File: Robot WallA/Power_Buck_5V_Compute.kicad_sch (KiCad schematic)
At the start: 13 parts

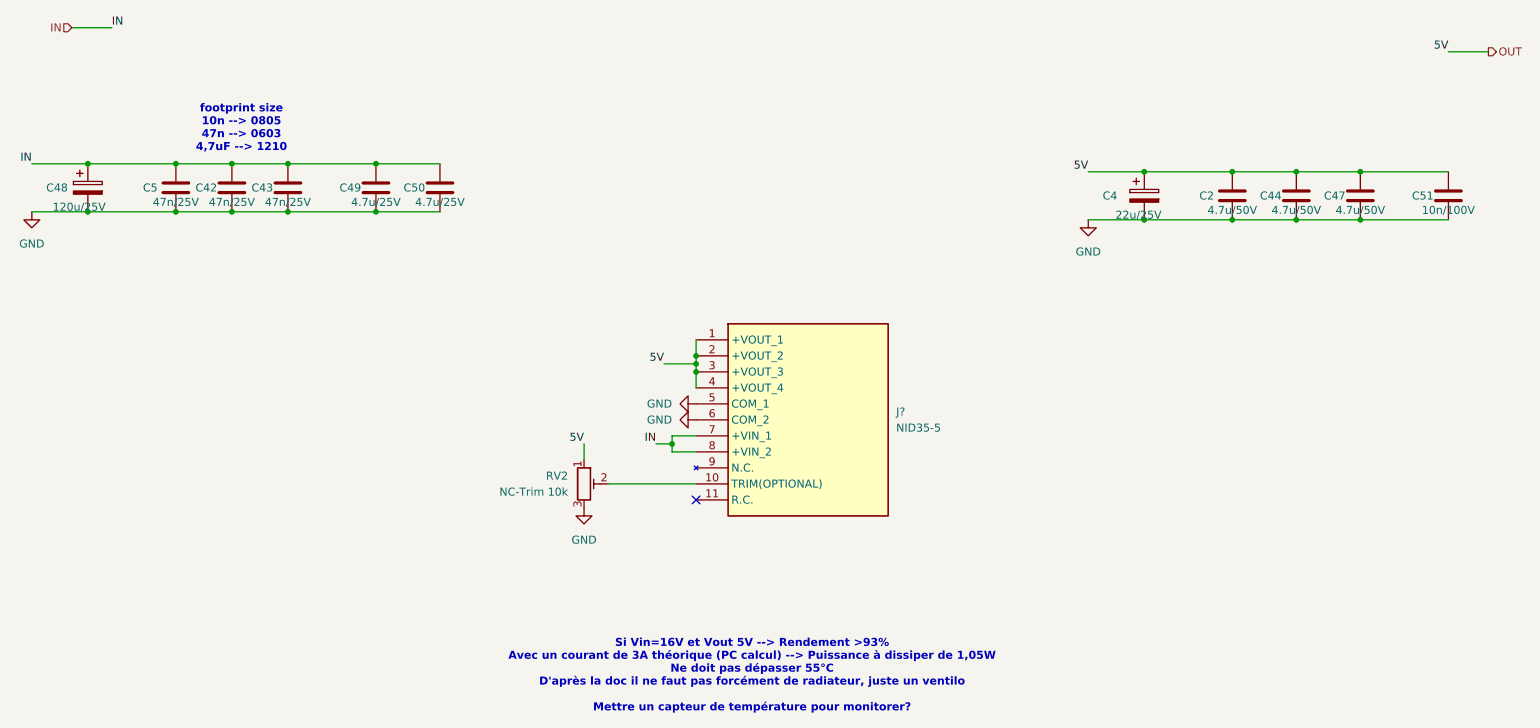
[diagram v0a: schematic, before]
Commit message: Continued to link MCU pins, Added a sheet for servomotors and optional 2 DC motors.
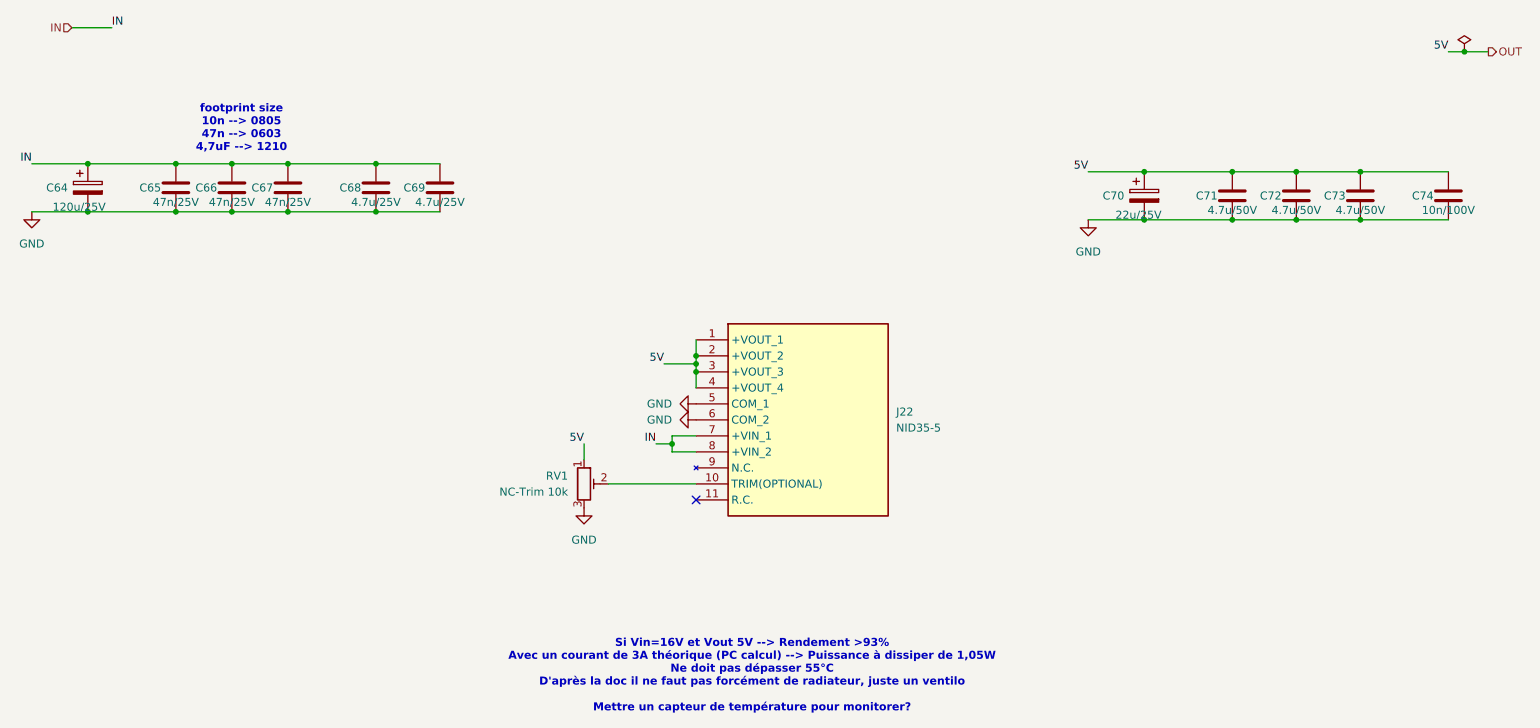
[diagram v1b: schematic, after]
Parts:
- removed C2, C44, C47: 4.7u/50V, symbol Device:C
- removed C4: 22u/25V, symbol Device:C_Polarized
- removed C42, C43, C5: 47n/25V, symbol Device:C
- removed C48: 120u/25V, symbol Device:C_Polarized
- removed C49, C50: 4.7u/25V, symbol Device:C
- removed C51: 10n/100V, symbol Device:C
- removed J?: NID35-5, NID355, symbol SamacSys_Parts:NID35-5
- removed RV2: NC-Trim 10k, symbol Device:R_Potentiometer_Trim
- added C64: 120u/25V, symbol Device:C_Polarized
- added C65, C66, C67: 47n/25V, symbol Device:C
- added C68, C69: 4.7u/25V, symbol Device:C
- added C70: 22u/25V, symbol Device:C_Polarized
- added C71, C72, C73: 4.7u/50V, symbol Device:C
- added C74: 10n/100V, symbol Device:C
- added J22: NID35-5, NID355, symbol SamacSys_Parts:NID35-5
- added RV1: NC-Trim 10k, symbol Device:R_Potentiometer_Trim
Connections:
- net GND: now also C64.2, C65.2, C66.2, C67.2, C68.2, C69.2, C70.2, C71.2, C72.2, C73.2, C74.2, J22.5 (COM_1), J22.6 (COM_2), RV1.3
- net IN: now also C64.1, C65.1, C66.1, C67.1, C68.1, C69.1, J22.7 (+VIN_1), J22.8 (+VIN_2)
- net OUT: now also C70.1, C71.1, C72.1, C73.1, C74.1, J22.1 (+VOUT_1), J22.2 (+VOUT_2), J22.3 (+VOUT_3), J22.4 (+VOUT_4), RV1.1
- new net: J22.10 (TRIM(OPTIONAL)), RV1.2

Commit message: Defined every footprints
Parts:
- C40: renamed from C64; value 120u/25V -> 120uF/25V; footprint (none) -> SamacSys_Parts:EEE0JA331XP; Manufacturer_Part_Number (none) -> EEE-FNV121XUP
- C41: renamed from C65; value 47n/25V -> 47nF/25V; footprint (none) -> Capacitor_SMD:C_0603_1608Metric_Pad1.08x0.95mm_HandSolder
- C42: renamed from C66; value 47n/25V -> 47nF/25V; footprint (none) -> Capacitor_SMD:C_0603_1608Metric_Pad1.08x0.95mm_HandSolder
- C43: renamed from C67; value 47n/25V -> 47nF/25V; footprint (none) -> Capacitor_SMD:C_0603_1608Metric_Pad1.08x0.95mm_HandSolder
- C44: renamed from C68; value 4.7u/25V -> 4.7uF/25V; footprint (none) -> Capacitor_SMD:C_1210_3225Metric_Pad1.33x2.70mm_HandSolder
- C45: renamed from C69; value 4.7u/25V -> 4.7uF/25V; footprint (none) -> Capacitor_SMD:C_1210_3225Metric_Pad1.33x2.70mm_HandSolder
- C46: renamed from C70; value 22u/25V -> 22uF/25V; footprint (none) -> Capacitor_SMD:C_0805_2012Metric_Pad1.18x1.45mm_HandSolder
- C47: renamed from C71; value 4.7u/50V -> 4.7uF/50V; footprint (none) -> Capacitor_SMD:C_0805_2012Metric_Pad1.18x1.45mm_HandSolder
- C48: renamed from C72; value 4.7u/50V -> 4.7uF/50V; footprint (none) -> Capacitor_SMD:C_0805_2012Metric_Pad1.18x1.45mm_HandSolder
- C49: renamed from C73; value 4.7u/50V -> 4.7uF/50V; footprint (none) -> Capacitor_SMD:C_0805_2012Metric_Pad1.18x1.45mm_HandSolder
- C50: renamed from C74; value 10n/100V -> 10nF/50V; footprint (none) -> Capacitor_SMD:C_0805_2012Metric_Pad1.18x1.45mm_HandSolder
- J11: renamed from J22; footprint NID355 -> SamacSys_Parts:NID355; Arrow Part Number NID35-5 -> (none); Arrow Price/Stock https://www.arrow.com/en/products/nid35-5/mean-well-enterpr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 -> (none); Height 13 -> (none); Manufacturer_Name Mean Well -> (none); Mouser Part Number 709-NID35-5 -> (none); Mouser Price/Stock https://www.mouser.co.uk/ProductDetail/MEAN-WELL/NID35-5?qs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 -> (none)
- RV1: value NC-Trim 10k -> Trim 10k; footprint (none) -> SamacSys_Parts:TC33X2503E; now not fitted

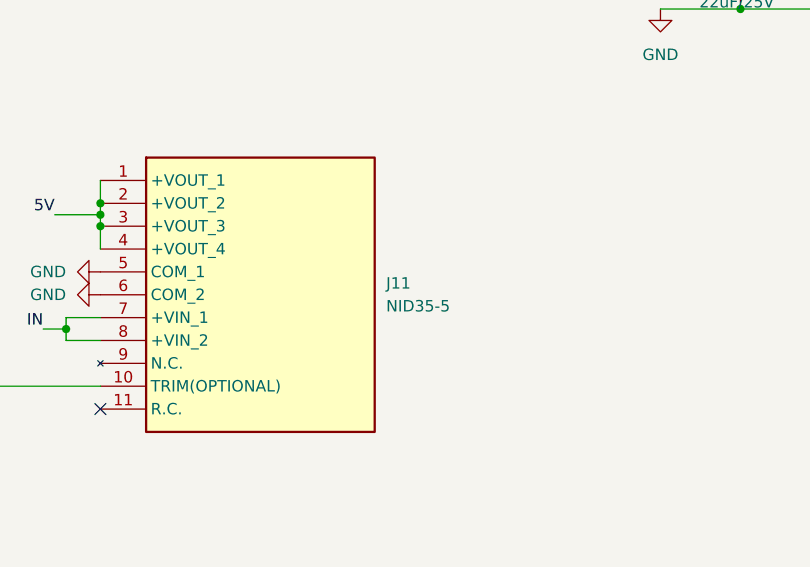
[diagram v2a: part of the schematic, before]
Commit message: Updated USB UART converter, Linked telemeter sensors.
Updated components indicators
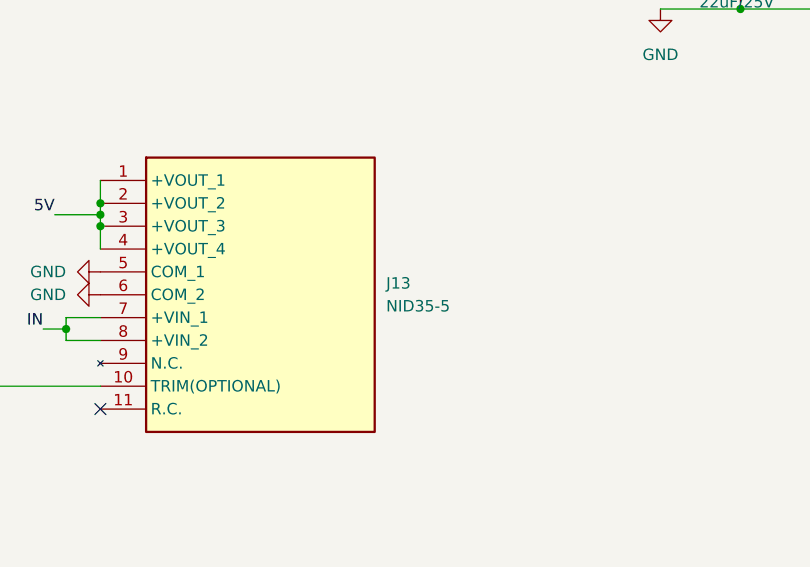
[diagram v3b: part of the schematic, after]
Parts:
- RV1: Manufacturer_Part_Number (none) -> TC33X2503E
- renumbered J11 to J13
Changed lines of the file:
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@@
+			)
+		)
+		(property "Manufacturer_Part_Number" "TC33X2503E"
+			(at 120.65 97.79 0)
+			(effects
+				(font
+					(size 1.27 1.27)
+				)
+				(hide yes)
 			)
 		)
@@
 		(dnp no)
 		(fields_autoplaced yes)
-		(property "Reference" "#PWR057"
+		(property "Reference" "#PWR059"
 			(at 132.08 87.63 0)
 			(effects
@@
 			(project "PCB"
 				(path "/117fd49e-499d-4b54-b58c-f6b538ecca4a/d5f4dab0-e2de-4083-971d-4b1eb9c8d4bb/690dff04-39a8-47af-a544-90bdf7825c98"
-					(reference "#PWR057")
+					(reference "#PWR059")
 					(unit 1)
 				)
@@
 		(dnp no)
 		(fields_autoplaced yes)
-		(property "Reference" "#PWR058"
+		(property "Reference" "#PWR060"
 			(at 120.65 107.95 0)
 			(effects
@@
 			(project "PCB"
 				(path "/117fd49e-499d-4b54-b58c-f6b538ecca4a/d5f4dab0-e2de-4083-971d-4b1eb9c8d4bb/690dff04-39a8-47af-a544-90bdf7825c98"
-					(reference "#PWR058")
+					(reference "#PWR060")
 					(unit 1)
 				)
@@
 		(dnp no)
 		(fields_autoplaced yes)
-		(property "Reference" "#PWR054"
+		(property "Reference" "#PWR056"
 			(at 33.02 60.96 0)
 			(effects
@@
 			(project "PCB"
 				(path "/117fd49e-499d-4b54-b58c-f6b538ecca4a/d5f4dab0-e2de-4083-971d-4b1eb9c8d4bb/690dff04-39a8-47af-a544-90bdf7825c98"
-					(reference "#PWR054")
+					(reference "#PWR056")
 					(unit 1)
 				)
@@
 		(dnp no)
 		(fields_autoplaced yes)
-		(property "Reference" "J11"
+		(property "Reference" "J13"
 			(at 170.18 86.3599 0)
 			(effects
@@
 			(project "PCB"
 				(path "/117fd49e-499d-4b54-b58c-f6b538ecca4a/d5f4dab0-e2de-4083-971d-4b1eb9c8d4bb/690dff04-39a8-47af-a544-90bdf7825c98"
-					(reference "J11")
+					(reference "J13")
 					(unit 1)
 				)
@@
 		(dnp no)
 		(fields_autoplaced yes)
-		(property "Reference" "#PWR056"
+		(property "Reference" "#PWR058"
 			(at 132.08 85.09 0)
 			(effects
@@
 			(project "PCB"
 				(path "/117fd49e-499d-4b54-b58c-f6b538ecca4a/d5f4dab0-e2de-4083-971d-4b1eb9c8d4bb/690dff04-39a8-47af-a544-90bdf7825c98"
-					(reference "#PWR056")
+					(reference "#PWR058")
 					(unit 1)
 				)
@@
 		(dnp no)
 		(fields_autoplaced yes)
-		(property "Reference" "#PWR055"
+		(property "Reference" "#PWR057"
 			(at 200.66 62.23 0)
 			(effects
@@
 			(project "PCB"
 				(path "/117fd49e-499d-4b54-b58c-f6b538ecca4a/d5f4dab0-e2de-4083-971d-4b1eb9c8d4bb/690dff04-39a8-47af-a544-90bdf7825c98"
-					(reference "#PWR055")
-					(unit 1)
-				)
+					(reference "#PWR057")
+					(unit 1)
+				)

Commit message: Continue to route
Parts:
- C46: footprint Capacitor_SMD:C_0805_2012Metric_Pad1.18x1.45mm_HandSolder -> SamacSys_Parts:EEE1AA220WR; Height (none) -> 5.5; Manufacturer_Part_Number (none) -> EEE-FN1E220R

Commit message: Reworked 12V and 5V power supplies, continue routing
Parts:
- removed C40: 120uF/25V, SamacSys_Parts:EEE0JA331XP, symbol Device:C_Polarized
- removed C41, C42, C43: 47nF/25V, Capacitor_SMD:C_0603_1608Metric_Pad1.08x0.95mm_HandSolder, symbol Device:C
- removed C44, C45: 4.7uF/25V, Capacitor_SMD:C_1210_3225Metric_Pad1.33x2.70mm_HandSolder, symbol Device:C
- removed C46: 22uF/25V, SamacSys_Parts:EEE1AA220WR, symbol Device:C_Polarized
- removed C47, C48, C49: 4.7uF/50V, Capacitor_SMD:C_0805_2012Metric_Pad1.18x1.45mm_HandSolder, symbol Device:C
- removed C50: 10nF/50V, Capacitor_SMD:C_0805_2012Metric_Pad1.18x1.45mm_HandSolder, symbol Device:C
- removed J13: NID35-5, SamacSys_Parts:NID355, symbol SamacSys_Parts:NID35-5
- removed RV1: Trim 10k, SamacSys_Parts:TC33X2503E, symbol Device:R_Potentiometer_Trim
- added C51: 330uF, SamacSys_Parts:CAPPRD500W65D1000H1800, symbol Device:C_Polarized
- added C52, C53: 4.7uF/50V, Capacitor_SMD:C_1210_3225Metric_Pad1.33x2.70mm_HandSolder, symbol Device:C
- added C54: 10nF/50V, Capacitor_SMD:C_0805_2012Metric_Pad1.18x1.45mm_HandSolder, symbol Device:C
- added C55: 2.2uF/50V, Capacitor_SMD:C_1210_3225Metric_Pad1.33x2.70mm_HandSolder, symbol Device:C
- added C56, C57, C58: 47nF/25V, Capacitor_SMD:C_0603_1608Metric_Pad1.08x0.95mm_HandSolder, symbol Device:C
- added C59, C60: 4.7uF/25V, Capacitor_SMD:C_1210_3225Metric_Pad1.33x2.70mm_HandSolder, symbol Device:C
- added D16: LED_RED, LED_SMD:LED_0603_1608Metric, symbol Device:LED
- added JP14: Closed, Jumper:SolderJumper-2_P1.3mm_Bridged_RoundedPad1.0x1.5mm, symbol Jumper:Jumper_2_Bridged
- added JP15: Open, Jumper:SolderJumper-2_P1.3mm_Open_RoundedPad1.0x1.5mm, symbol Jumper:Jumper_2_Open
- added Q1: BSS138, Package_TO_SOT_SMD:SOT-23, symbol Transistor_FET:BSS138
- added R31: 1.6k, Resistor_SMD:R_0603_1608Metric_Pad0.98x0.95mm_HandSolder, symbol Device:R
- added R32: 21k, Resistor_SMD:R_0603_1608Metric_Pad0.98x0.95mm_HandSolder, symbol Device:R
- added R40: 10k, Resistor_SMD:R_0603_1608Metric_Pad0.98x0.95mm_HandSolder, symbol Device:R
- added RV2: Trim 2k, SamacSys_Parts:TC42X2202E, symbol Device:R_Potentiometer_Trim
- added U10: PTN78060W_EUW-7, Module:Texas_EUW_R-PDSS-T7_THT, symbol Converter_DCDC:PTN78060W_EUW-7
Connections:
- net GND: now also C51.2, C52.2, C53.2, C54.2, C55.2, C56.2, C57.2, C58.2, C59.2, C60.2, JP14.1 (A), Q1.2 (S), R31.2, R40.2, RV2.2, U10.1 (GND), U10.7 (GND)
- net IN: now also C55.1, C56.1, C57.1, C58.1, C59.1, C60.1, U10.2 (VI)
- net OUT: now also C51.1, C52.1, C53.1, C54.1, D16.2 (A), U10.5 (VO_Sense), U10.6 (VO)
- new net: JP15.2 (B), RV2.1
- new net: D16.1 (K), R31.1
- new net: JP14.2 (B), JP15.1 (A), R32.2
- new net: Q1.3 (D), U10.3 (~{Inhibit})
- new net GPIO_ENABLE: Q1.1 (G), R40.1
- new net TRIM: R32.1, U10.4 (VO_Adj)
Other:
- note removed: "Si Vin=16V et Vout 5V --> Rendement >93% Avec un courant de 3A théorique (PC calcul) --> Puissance à dissiper de 1,05W Ne doit pas dépasser 55°C D'après la doc il ne faut pas forcément de radiateur, juste un ventilo Mettre un capteur de température pour monitorer?"
- note removed: "footprint size 10n --> 0805 47n --> 0603 4,7uF --> 1210"

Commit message: Correct a lot of error in DRC
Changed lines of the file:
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@@
-	)
-	(junction
-		(at 260.35 29.21)
-		(diameter 0)
-		(color 0 0 0 0)
 	)
 	(junction
@@
 	(wire
 		(pts
-			(xy 257.81 29.21) (xy 260.35 29.21)
+			(xy 257.81 29.21) (xy 264.16 29.21)
 		)
 		(stroke
@@
 		(pts
 			(xy 115.57 114.3) (xy 125.73 114.3)
-		)
-		(stroke
-			(width 0)
-			(type default)
-		)
-	)
-	(wire
-		(pts
-			(xy 260.35 29.21) (xy 264.16 29.21)
 		)
 		(stroke
@@
 	(symbol
 		(lib_id "power:PWR_FLAG")
-		(at 260.35 29.21 0)
+		(at 50.8 48.26 0)
 		(unit 1)
 		(exclude_from_sim no)
@@
 		(fields_autoplaced yes)
 		(property "Reference" "#FLG04"
-			(at 260.35 27.305 0)
+			(at 50.8 46.355 0)
 			(effects
 				(font
@@
 		)
 		(property "Value" "PWR_FLAG"
-			(at 260.35 24.13 0)
+			(at 50.8 43.18 0)
 			(effects
 				(font
@@
 		)
 		(property "Footprint" ""
-			(at 260.35 29.21 0)
+			(at 50.8 48.26 0)
 			(effects
 				(font
@@
 		)
 		(property "Datasheet" "~"
-			(at 260.35 29.21 0)
+			(at 50.8 48.26 0)
 			(effects
 				(font
@@
 		)
 		(property "Description" "Special symbol for telling ERC where power comes from"
-			(at 260.35 29.21 0)
-			(effects
-				(font
+			(at 50.8 48.26 0)
+			(effects
+				(font

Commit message: Corrected all DRC erros, added info on PCB
modified distance meter connectors to be horizontal
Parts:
- C51: value 330uF -> 100uF; footprint SamacSys_Parts:CAPPRD500W65D1000H1800 -> SamacSys_Parts:CAPPRD350W65D800H1250; Manufacturer_Part_Number EEU-FC1V331 -> (none)
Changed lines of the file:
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@@
 			)
 		)
-		(property "Value" "330uF"
+		(property "Value" "100uF"
 			(at 225.044 53.086 0)
 			(effects
@@
 			)
 		)
-		(property "Footprint" "SamacSys_Parts:CAPPRD500W65D1000H1800"
+		(property "Footprint" "SamacSys_Parts:CAPPRD350W65D800H1250"
 			(at 225.7552 54.61 0)
 			(effects
@@
 			)
 		)
-		(property "Manufacturer_Part_Number" "EEU-FC1V331"
+		(property "Manufacturer_Part_Number" ""
 			(at 224.79 50.8 0)
 			(effects

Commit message: Updated fab files.
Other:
- company: (none) -> Socotec Monitoring
- title: (none) -> Robot Wall-A
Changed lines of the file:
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@@
 	(generator_version "9.0")
 	(paper "A4")
+	(title_block
+		(title "Robot Wall-A")
+		(date "2025-09-20")
+		(rev "v1.0")
+		(company "Socotec Monitoring")
+		(comment 1 "GDU")
+		(comment 2 "THO")
+	)
 	(junction
 		(at 63.5 48.26)
@@
 			)
 		)
+		(property "MPN" ""
+			(at 81.28 52.07 0)
+			(effects
+				(font
+					(size 1.27 1.27)
+				)
+				(hide yes)
+			)
+		)
 		(pin "1"
 		)
@@
 			)
 		)
+		(property "MPN" ""
+			(at 256.54 125.73 0)
+			(effects
+				(font
+					(size 1.27 1.27)
+				)
+				(hide yes)
+			)
+		)
 		(pin "2"
 		)
@@
 			)
 		)
+		(property "MPN" ""
+			(at 154.94 52.07 0)
+			(effects
+				(font
+					(size 1.27 1.27)
+				)
+				(hide yes)
+			)
+		)
 		(pin "2"
 		)
@@
 			)
 		)
+		(property "MPN" ""
+			(at 50.8 52.07 0)
+			(effects
+				(font
+					(size 1.27 1.27)
+				)
+				(hide yes)
+			)
+		)
 		(pin "1"
 		)
@@
 			)
 		)
+		(property "MPN" ""
+			(at 256.54 116.84 90)
+			(effects
+				(font
+					(size 1.27 1.27)
+				)
+				(hide yes)
+			)
+		)
 		(pin "1"
 		)
@@
 			)
 		)
+		(property "MPN" ""
+			(at 105.41 52.07 0)
+			(effects
+				(font
+					(size 1.27 1.27)
+				)
+				(hide yes)
+			)
+		)
 		(pin "1"
 		)
@@
 			)
 		)
+		(property "MPN" ""
+			(at 63.5 52.07 0)
+			(effects
+				(font
+					(size 1.27 1.27)
+				)
+				(hide yes)
+			)
+		)
 		(pin "1"
 		)
@@
 			)
 		)
+		(property "MPN" ""
+			(at 238.76 50.8 0)
+			(effects
+				(font
+					(size 1.27 1.27)
+				)
+				(hide yes)
+			)
+		)
 		(pin "1"
 		)
@@
 			)
 		)
+		(property "MPN" ""
+			(at 224.79 50.8 0)
+			(effects
+				(font
+					(size 1.27 1.27)
+				)
+				(hide yes)
+			)
+		)
 		(pin "1"
 		)
@@
 			)
 		)
+		(property "MPN" ""
+			(at 115.57 110.49 90)
+			(effects
+				(font
+					(size 1.27 1.27)
+				)
+				(hide yes)
+			)
+		)
 		(pin "1"
 		)
@@
 			)
 		)
+		(property "MPN" ""
+			(at 262.89 50.8 0)
+			(effects
+				(font
+					(size 1.27 1.27)
+				)
+				(hide yes)
+			)
+		)
 		(pin "1"
 		)
@@
 			)
 		)
+		(property "MPN" ""
+			(at 246.38 116.84 90)
+			(effects
+				(font
+					(size 1.27 1.27)
+				)
+				(hide yes)
+			)
+		)
 		(pin "2"
 		)
@@
 			)
 		)
+		(property "MPN" ""
+			(at 72.39 52.07 0)
+			(effects
+				(font
+					(size 1.27 1.27)
+				)
+				(hide yes)
+			)
+		)
 		(pin "1"
 		)
@@
 			)
 		)
+		(property "MPN" ""
+			(at 251.46 107.95 0)
+			(effects
+				(font
+					(size 1.27 1.27)
+				)
+				(hide yes)
+			)
+		)
 		(pin "1"
 		)
@@
 			)
 		)
+		(property "MPN" ""
+			(at 95.25 52.07 0)
+			(effects
+				(font
+					(size 1.27 1.27)
+				)
+				(hide yes)
+			)
+		)
 		(pin "1"
 		)
@@
 			)
 		)
+		(property "MPN" ""
+			(at 248.92 50.8 0)
+			(effects
+				(font
+					(size 1.27 1.27)
+				)
+				(hide yes)
+			)
+		)
 		(pin "1"
 		)
@@
 			)
 		)
+		(property "MPN" ""
+			(at 165.1 52.07 90)
+			(effects
+				(font
+					(size 1.27 1.27)
+				)
+				(hide yes)
+			)
+		)
 		(pin "1"
 		)
@@
 			)
 		)
+		(property "MPN" ""
+			(at 123.19 105.41 0)
+			(effects
+				(font
+					(size 1.27 1.27)
+				)
+				(hide yes)
+			)
+		)
 		(pin "2"
 		)
@@
 			(at 148.59 100.33 0)
 			(effects
+				(font
+					(size 1.27 1.27)
+				)
+				(hide yes)
+			)
+		)
+		(property "MPN" ""
+			(at 148.59 100.33 0)
+			(effects
